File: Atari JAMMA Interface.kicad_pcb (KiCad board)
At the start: 2 copper layers, 112.2 x 74.8 mm, 45 parts, among them P1 10K, U1 LM386, U2 DIP-14_W7.62mm, U3 MC34063AP, U4 74LS04

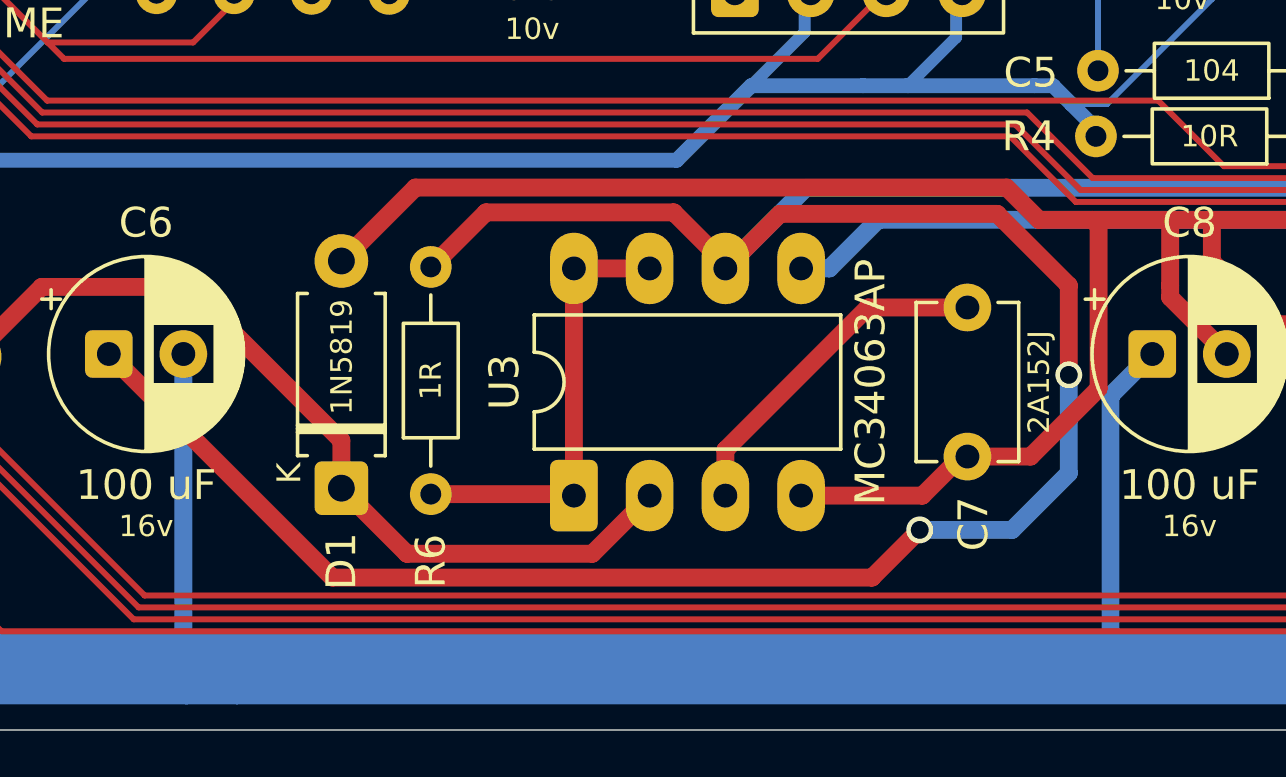
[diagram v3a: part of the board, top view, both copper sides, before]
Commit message: 3.4mm film caps for 152
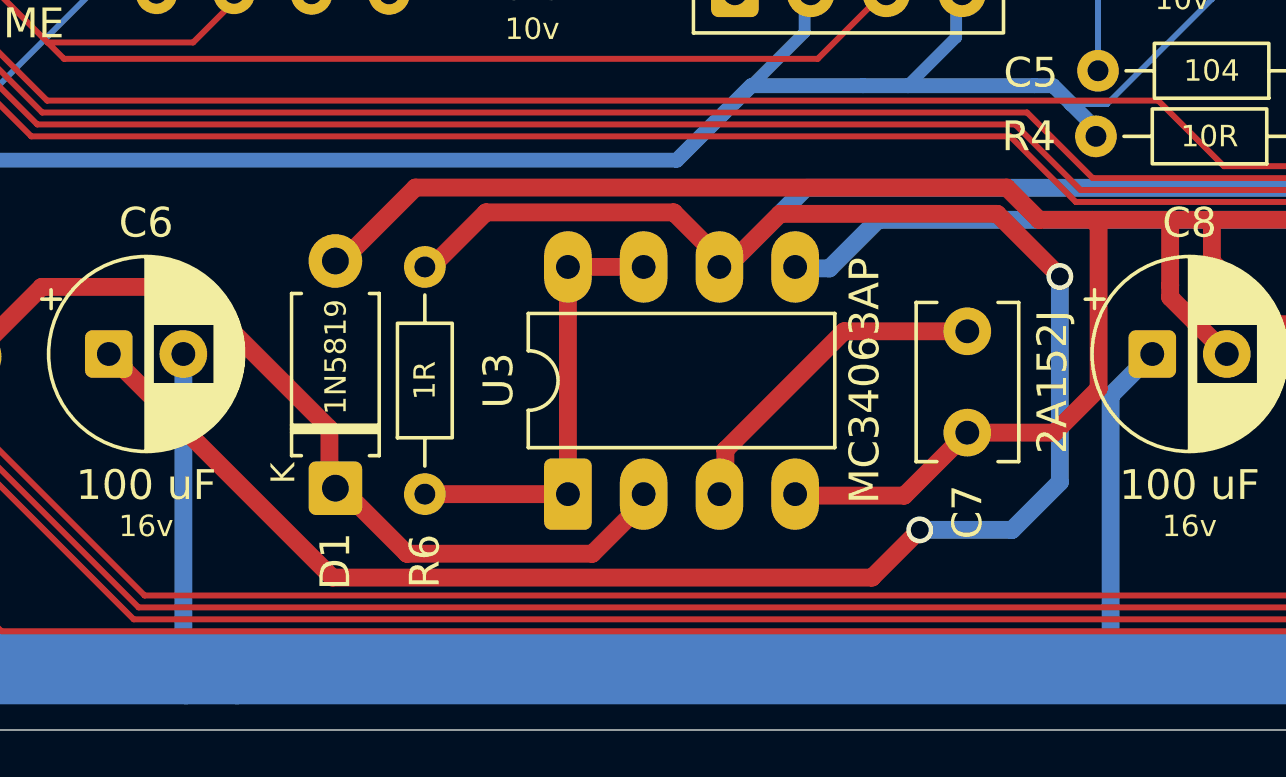
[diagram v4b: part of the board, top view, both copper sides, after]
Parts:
- C7: footprint Capacitor_THT:C_Disc_D5.1mm_W3.2mm_P5.00mm -> Capacitor_THT:C_Disc_D5.1mm_W3.2mm_P3.4mm
- moved U3 0.21 mm to (133.6, 130.2)
- moved D1 0.20 mm to (125.8, 130.0)
- moved R6 0.20 mm to (128.8, 130.2)
